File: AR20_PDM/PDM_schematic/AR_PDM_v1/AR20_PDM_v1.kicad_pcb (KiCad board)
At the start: 2 copper layers, 128 x 122 mm, 284 parts, among them J1 S_T_?, J2 1-776163-1, K1 DIPxx-1Cxx-51x, K2 DIPxx-1Cxx-51x, P1 B4B-PH-SM4-TB, Q1 BTS50025-1TAD, Q2 BTS50025-1TAD, Q3 BTS50025-1TAD, Q5 BTS50025-1TAD, Q6 BTS50025-1TAD, Q7 BTS50025-1TAD, Q8 BTS50025-1TAD, SW1 SW_DIP_x07, U1 ACM_2020, U10 N-MOS, U11 N-MOS, U12 P-MOS, U13 N-MOS, U14 N-MOS, U15 NMOS, U16 NMOS, U17 NMOS, U18 NMOS, U19 NMOS, U2 INA233, U20 NMOS, U21 NMOS, U22 NMOS, U23 NMOS, U24 NMOS, U25 NMOS, U26 NMOS, U27 NMOS, U28 NMOS, U29 INA233, U3 INA233, U30 INA233, U31 INA233, U32 Fet-P, U33 Fet-P, U34 Fet-P, U35 Fet-P, U36 Fet-P, U37 P-MOS-SIRA99DP-T1-GE3, U38 P-MOS-SIRA99DP-T1-GE3, U39 P-MOS-SIRA99DP-T1-GE3, U4 INA233, U40 P-MOS-SIRA99DP-T1-GE3, U41 P-MOS-SIRA99DP-T1-GE3, U5 INA233, U6 INA233, U7 INA233, U8 INA233, U9 TCA6424ARGJR

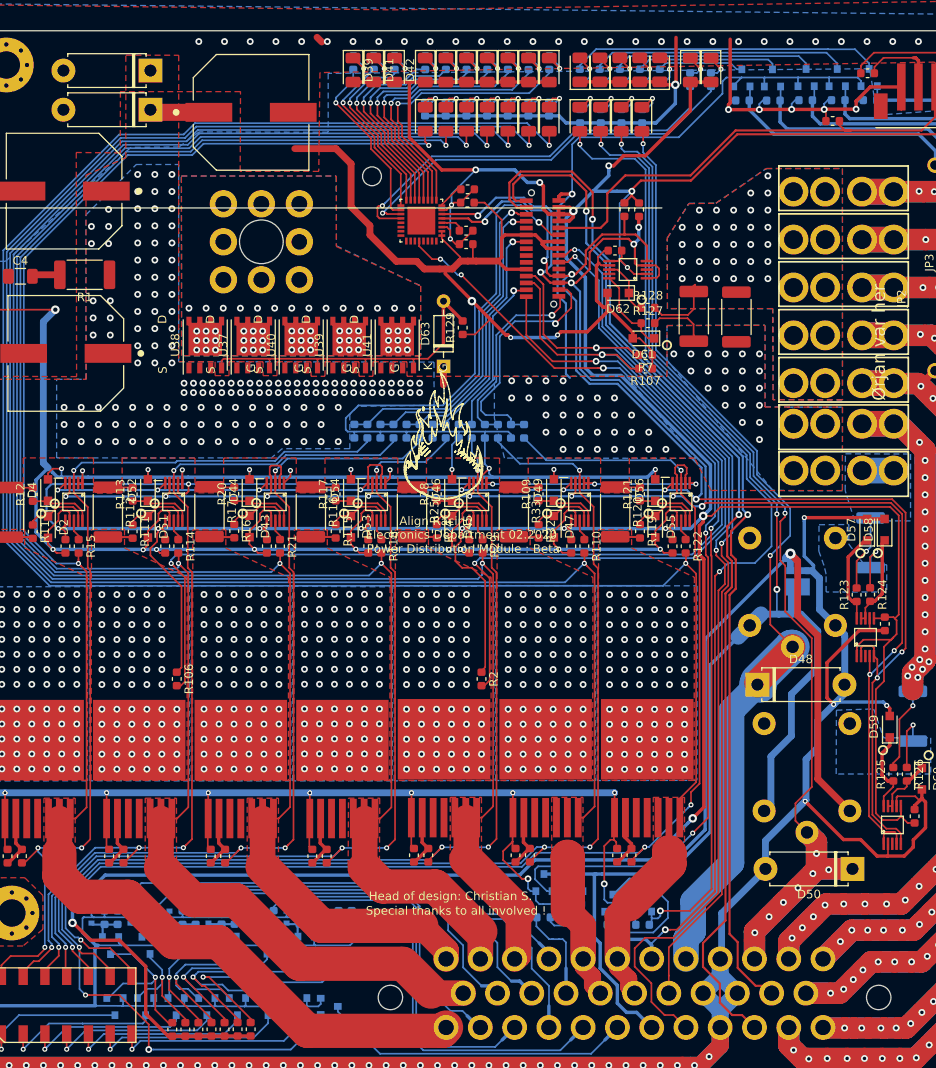
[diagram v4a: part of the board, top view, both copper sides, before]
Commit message: Mostly finalized
- Fixed alot of the masking
- Replaced main Flyback diodes to shotky type with low VF
- Fix DRC one footprint still to small clearance
- Fix silkscreen
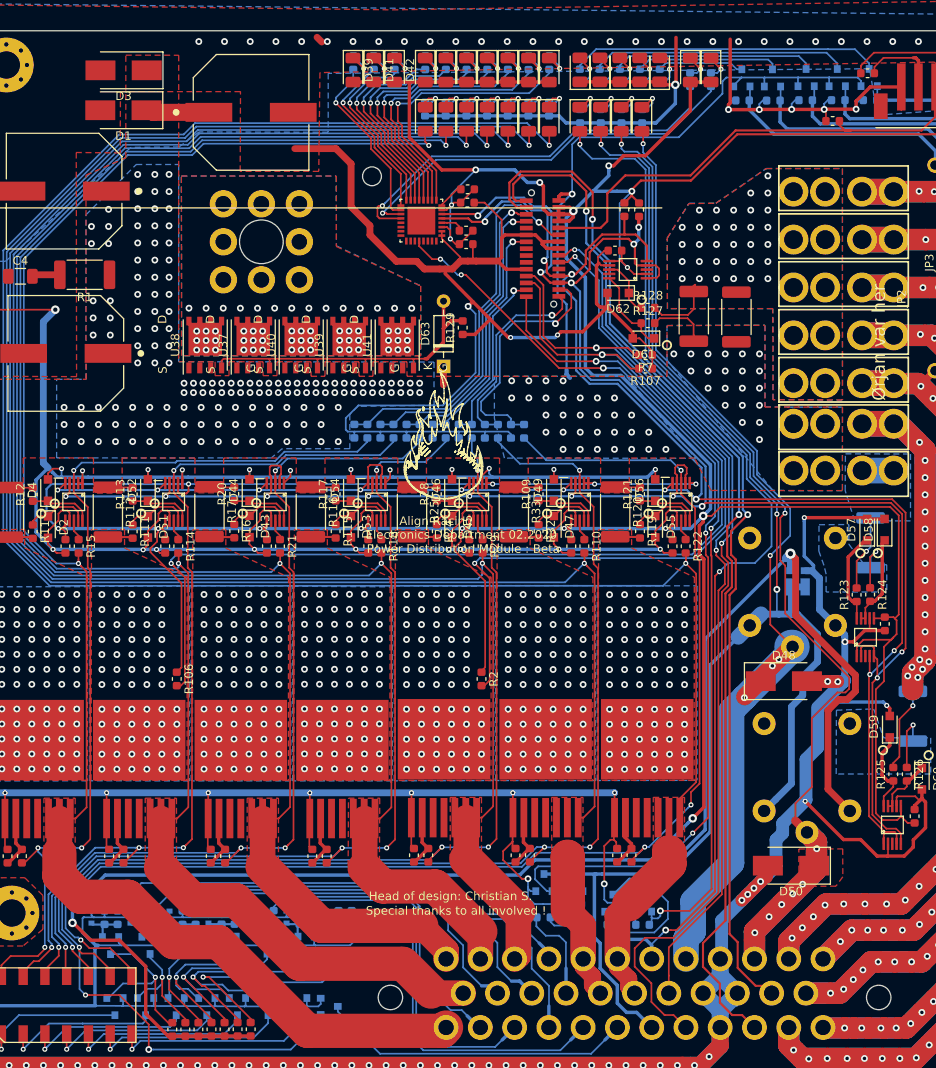
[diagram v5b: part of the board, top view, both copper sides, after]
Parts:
- D1, D3, D48, D50: footprint Diode_THT:D_5W_P10.16mm_Horizontal -> Diode_SMD:D_SMB_Handsoldering
- moved D50 7.18 mm to (129.4, 123.8)
- moved D1 3.16 mm to (51.5, 35.6)
- moved D3 3.14 mm to (51.5, 31.0)
- moved D48 3.11 mm to (128.6, 102.3)
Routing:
- net FUEL_PUMP_OUT: track 138.5 -> 134.4 mm, vias 9 -> 8
- net FP_ENABLE_RELAY_SINK: track 114.1 -> 117.3 mm
- net GND: track 1240.3 -> 1238.5 mm, vias 164 -> 170
- net vcc_5v: track 675.7 -> 673.8 mm
- net COIL_INJECTOR_OUT: track 117.6 -> 119.3 mm, vias 2 -> 5
- added copper zone on F.Cu, net FUEL_PUMP_OUT

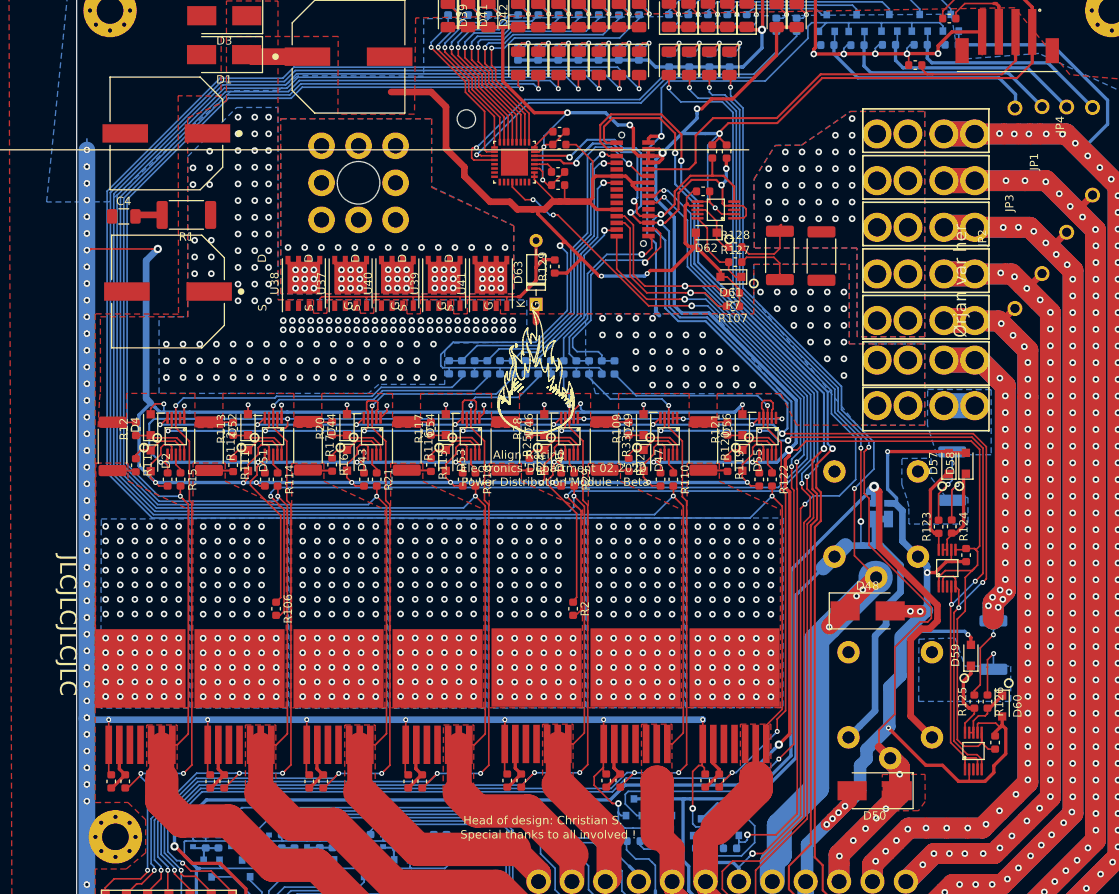
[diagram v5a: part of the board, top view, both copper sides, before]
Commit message: All done except port expander footprint
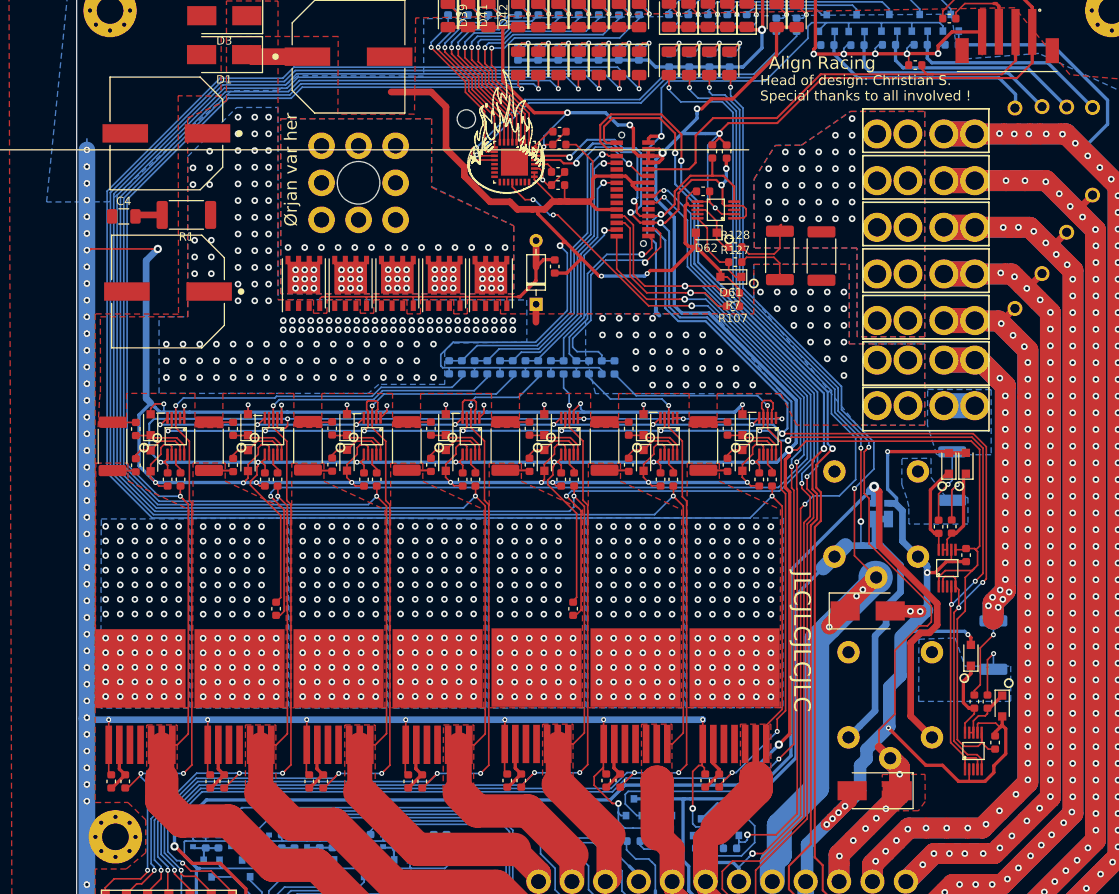
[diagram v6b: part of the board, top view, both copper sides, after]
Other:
- board text added: "Electronics Department 08.2020"
- board text added: "Power Distribution Module : Charlie"
- board text removed: "Electronics Department 02.2020"
- board text removed: "Fuel ACM"
- board text removed: "Fuel AUX"
- board text removed: "Pico SD"
- board text removed: "Power Distribution Module : Beta"

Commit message: PDM V 3 Charlie Finished, awaiting final inspection
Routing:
- net P6_OUT: track 223.5 -> 228.3 mm
- net P7_OUT: track 241.3 -> 245.1 mm
- net GND: track 1238.5 -> 1239.2 mm, vias 170 -> 171
